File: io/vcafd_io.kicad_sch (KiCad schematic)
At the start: 37 parts, among them J1 AudioJack2_SwitchT, J2 AudioJack2_SwitchT, J3 AudioJack2_SwitchT, J4 AudioJack2_SwitchT, J5 AudioJack2_SwitchT, J6 AudioJack2_SwitchT, J7 Conn_01x09_Pin, J8 Conn_01x09_Pin, J9 Conn_01x09_Pin, Q1 2N7002, Q2 2N7002, Q3 2N7002, Q4 2N7002, SW1 SW_SPDT, SW2 SW_SPDT

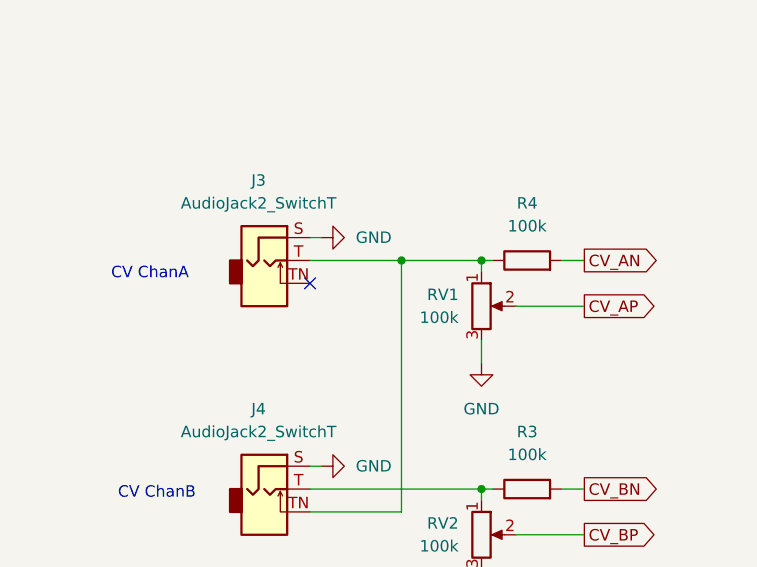
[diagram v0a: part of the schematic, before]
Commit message: Connect CV Tn to ground
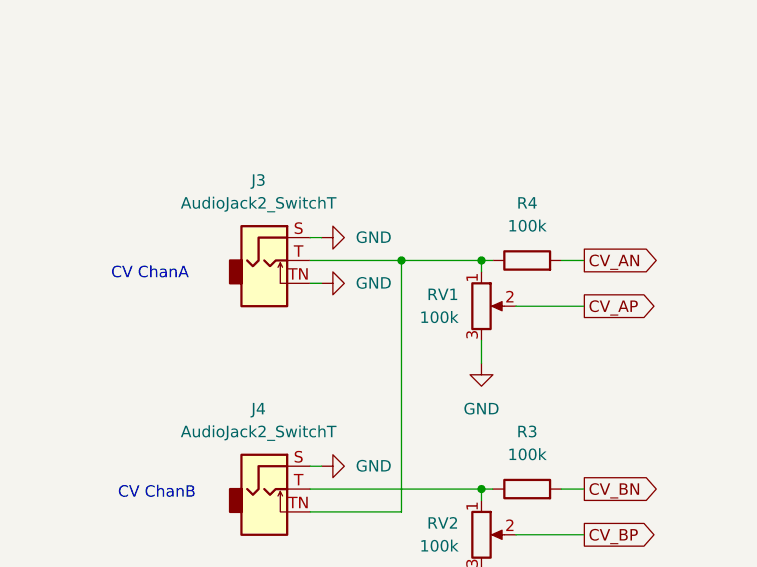
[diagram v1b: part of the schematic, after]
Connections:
- net GND: now also J3.TN
- no-connect marks 3 -> 2
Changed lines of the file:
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@@
 (kicad_sch
-	(version 20231120)
+	(version 20250114)
 	(generator "eeschema")
-	(generator_version "8.0")
+	(generator_version "9.0")
 	(paper "A4")
 	(title_block
@@
 		(rev "1.0")
 	)
+	(text "CV ChanA"
+		(exclude_from_sim no)
+		(at 35.56 103.124 0)
+		(effects
+			(font
+				(size 1.27 1.27)
+			)
+		)
+	)
+	(text "CV ChanB"
+		(exclude_from_sim no)
+		(at 36.322 127.508 0)
+		(effects
+			(font
+				(size 1.27 1.27)
+			)
+		)
+	)
+	(text "Input ChanB"
+		(exclude_from_sim no)
+		(at 35.052 65.278 0)
+		(effects
+			(font
+				(size 1.27 1.27)
+			)
+		)
+	)
+	(text "Input ChanA"
+		(exclude_from_sim no)
+		(at 34.544 40.132 0)
+		(effects
+			(font
+				(size 1.27 1.27)
+			)
+		)
+	)
 	(junction
 		(at 234.95 57.15)
@@
 		(at 241.3 130.81)
 	)
-	(no_connect
-		(at 53.34 104.14)
-	)
 	(wire
 		(pts
@@
 	(wire
 		(pts
+			(xy 54.61 104.14) (xy 53.34 104.14)
+		)
+		(stroke
+			(width 0)
+			(type default)
+		)
+	)
+	(wire
+		(pts
 			(xy 53.34 127) (xy 72.39 127)
 		)
@@
 		)
 	)
-	(text "CV ChanA"
-		(exclude_from_sim no)
-		(at 35.56 103.124 0)
-		(effects
-			(font
-				(size 1.27 1.27)
-			)
-		)
-	)
-	(text "CV ChanB"
-		(exclude_from_sim no)
-		(at 36.322 127.508 0)
-		(effects
-			(font
-				(size 1.27 1.27)
-			)
-		)
-	)
-	(text "Input ChanB"
-		(exclude_from_sim no)
-		(at 35.052 65.278 0)
-		(effects
-			(font
-				(size 1.27 1.27)
-			)
-		)
-	)
-	(text "Input ChanA"
-		(exclude_from_sim no)
-		(at 34.544 40.132 0)
-		(effects
-			(font
-				(size 1.27 1.27)
-			)
-		)
-	)
 	(global_label "CV_BP"
 		(shape input)
@@
 	)
 	(symbol
+		(lib_id "power:GND")
+		(at 54.61 104.14 90)
+		(unit 1)
+		(exclude_from_sim no)
+		(in_bom yes)
+		(on_board yes)
+		(dnp no)
+		(fields_autoplaced yes)
+		(property "Reference" "#PWR09"
+			(at 60.96 104.14 0)
+			(effects
+				(font
+					(size 1.27 1.27)
+				)
+				(hide yes)
+			)
+		)
+		(property "Value" "GND"
+			(at 58.42 104.1399 90)
+			(effects
+				(font
+					(size 1.27 1.27)
+				)
+				(justify right)
+			)
+		)
+		(property "Footprint" ""
+			(at 54.61 104.14 0)
+			(effects
+				(font
+					(size 1.27 1.27)
+				)
+				(hide yes)
+			)
+		)
+		(property "Datasheet" ""
+			(at 54.61 104.14 0)
+			(effects
+				(font
+					(size 1.27 1.27)
+				)
+				(hide yes)
+			)
+		)
+		(property "Description" "Power symbol creates a global label with name \"GND\" , ground"
+			(at 54.61 104.14 0)
+			(effects
+				(font
+					(size 1.27 1.27)
+				)
+				(hide yes)
+			)
+		)
+		(pin "1"
+		)
+		(instances
+			(project "vcafd_io"
+				(path "/01f65fda-f88a-43c5-aeac-b1854b45a639"
+					(reference "#PWR09")
+					(unit 1)
+				)
+			)
+		)
+	)
+	(symbol
 		(lib_id "Device:R_Potentiometer")
 		(at 72.39 132.08 0)
@@
 		)
 	)
+	(embedded_fonts no)
 )
